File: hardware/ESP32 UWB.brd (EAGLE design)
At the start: 72.3 x 32.6 mm, 54 parts, among them J2 HEADER-12P-2.54, J4 10118194-0001LF, Q3 S8050, Q4 S8050, U1 SILICON_LABS_CP2102N-A01-GQFN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, U2 V_REG_MIC2920, U5 DWM1000, U6 ESP32-C3-MINI-1-N4

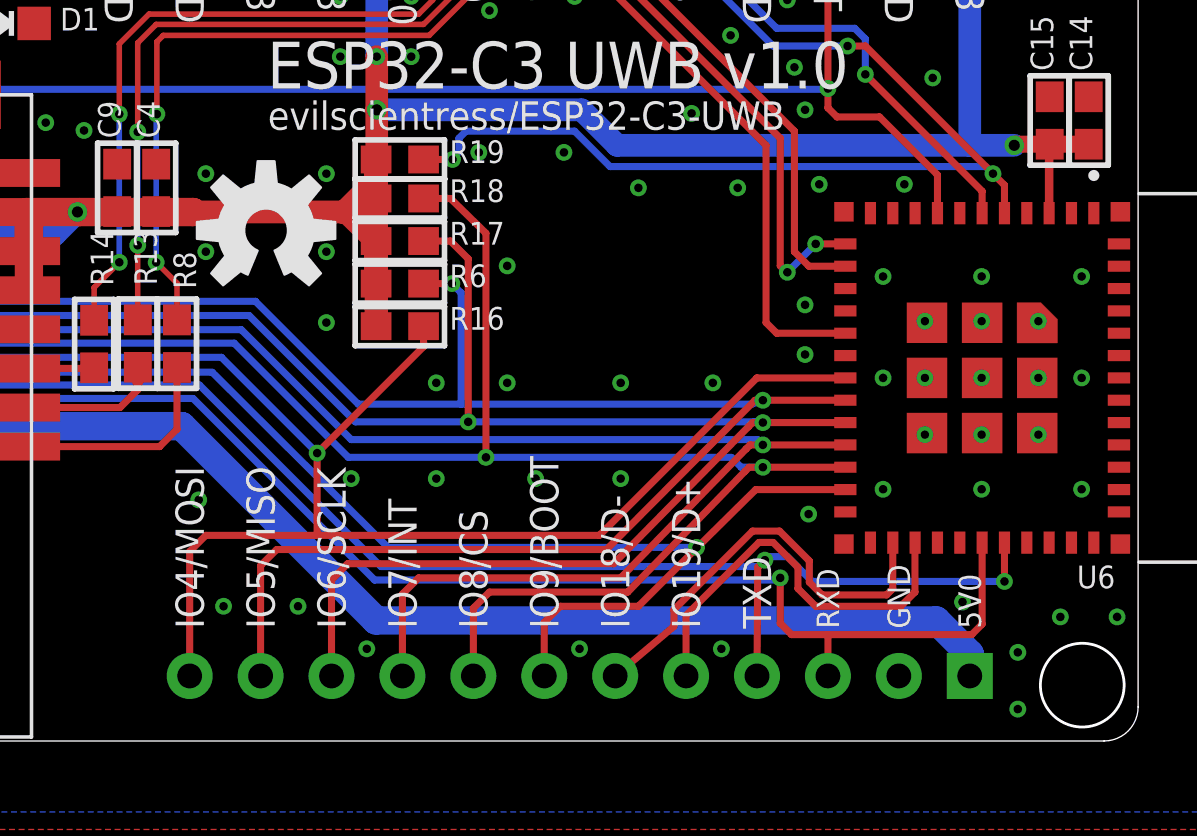
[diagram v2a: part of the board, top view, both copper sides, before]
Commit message: Added WS2812b led for status display
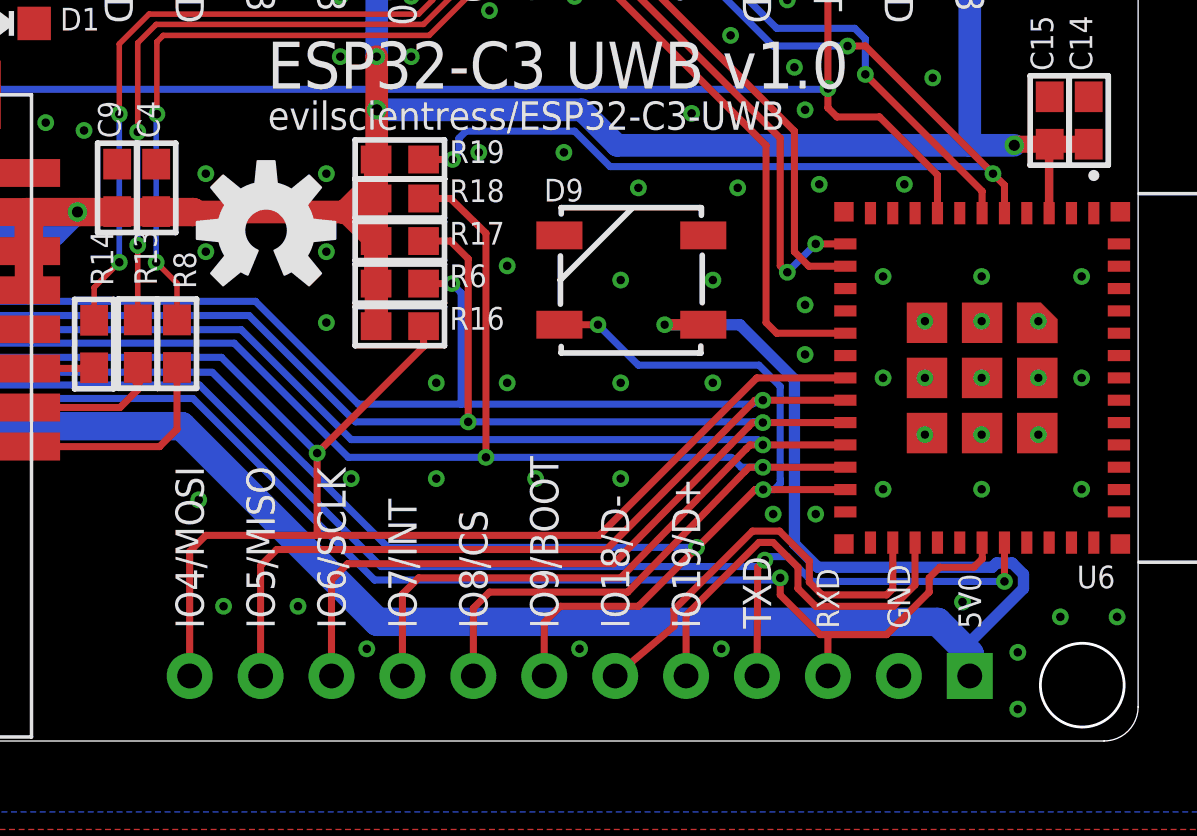
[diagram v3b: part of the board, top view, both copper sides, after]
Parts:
- added D9: (no value), SparkFun-LED:WS2812B
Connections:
- net GND: now also D9.3
- net IO9: now also D9.4
- net VDD5V: now also D9.1
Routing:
- net VDD5V: track 70.3 -> 95.5 mm, vias 1 -> 2
- net IO9: track 83.9 -> 96.9 mm, vias 2 -> 4
- net RXD: track 70.9 -> 69.2 mm
- net GND: vias 134 -> 137
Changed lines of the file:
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@@
 <setting verticaltext="up"/>
 </settings>
-<grid distance="10" unitdist="mil" unit="mil" style="dots" multiple="1" display="yes" altdistance="1" altunitdist="mil" altunit="mil"/>
+<grid distance="10" unitdist="mil" unit="mm" style="dots" multiple="1" display="yes" altdistance="1" altunitdist="mil" altunit="mil"/>
 <layers>
 <layer number="1" name="Top" color="4" fill="1" visible="yes" active="yes"/>
@@
 <attribute name="VALUE" x="3.81" y="10.16" size="0.4064" layer="27" font="vector" ratio="10" rot="R180"/>
 </element>
+<element name="D9" library="SparkFun-LED" package="WS2812B" value="" x="53.848" y="16.51" smashed="yes" rot="R180">
+<attribute name="PROD_ID" value="DIO-12503" x="53.848" y="16.51" size="1.016" layer="27" font="vector" ratio="18" rot="R180" display="off"/>
+<attribute name="NAME" x="52.134" y="20.136" size="0.8128" layer="25" font="vector" ratio="18" rot="R180"/>
+<attribute name="VALUE" x="49.594" y="18.11" size="0.6096" layer="27" rot="R180"/>
+</element>
 </elements>
 <signals>
@@
 <via x="7.493" y="20.193" extent="1-16" drill="0.3048"/>
 <via x="10.16" y="12.954" extent="1-16" drill="0.3048"/>
-<via x="60.198" y="8.128" extent="1-16" drill="0.3048"/>
+<via x="60.452" y="8.128" extent="1-16" drill="0.3048"/>
 <via x="65.7098" y="4.9784" extent="1-16" drill="0.3048"/>
 <via x="71.247" y="4.445" extent="1-16" drill="0.3048"/>
@@
 <contactref element="C5" pad="2"/>
 <contactref element="C7" pad="2"/>
+<contactref element="D9" pad="3"/>
+<via x="58.928" y="8.128" extent="1-16" drill="0.3048"/>
+<via x="56.769" y="16.51" extent="1-16" drill="0.3048"/>
+<via x="53.467" y="16.51" extent="1-16" drill="0.3048"/>
 </signal>
 <signal name="+3V3">
@@
 <wire x1="59.817" y1="6.223" x2="59.817" y2="5.461" width="0.254" layer="1"/>
 <wire x1="59.817" y1="5.461" x2="60.452" y2="4.826" width="0.254" layer="1"/>
-<wire x1="60.452" y1="4.826" x2="63.5" y2="4.826" width="0.254" layer="1"/>
-<wire x1="63.5" y1="4.826" x2="64.008" y2="5.334" width="0.254" layer="1"/>
-<wire x1="64.008" y1="5.334" x2="64.008" y2="7.0994" width="0.254" layer="1"/>
+<wire x1="60.452" y1="4.826" x2="63.246" y2="4.826" width="0.254" layer="1"/>
+<wire x1="63.246" y1="4.826" x2="64.008" y2="5.588" width="0.254" layer="1"/>
+<wire x1="64.008" y1="5.588" x2="64.008" y2="7.0994" width="0.254" layer="1"/>
 <wire x1="64.008" y1="7.0994" x2="64.0134" y2="7.1048" width="0.254" layer="1"/>
 </signal>
@@
 <wire x1="59.1058" y1="5.7658" x2="59.182" y2="5.842" width="0.254" layer="16"/>
 <via x="59.182" y="5.842" extent="1-16" drill="0.3048"/>
-<wire x1="59.182" y1="4.216" x2="59.182" y2="5.842" width="0.254" layer="1"/>
-<wire x1="66.4134" y1="7.1048" x2="66.4134" y2="4.1834" width="0.254" layer="1"/>
-<wire x1="66.4134" y1="4.1834" x2="66.04" y2="3.81" width="0.254" layer="1"/>
-<wire x1="66.04" y1="3.81" x2="60.89" y2="3.81" width="0.254" layer="1"/>
-<wire x1="60.89" y1="3.81" x2="59.588" y2="3.81" width="0.254" layer="1"/>
-<wire x1="59.182" y1="4.216" x2="59.588" y2="3.81" width="0.254" layer="1"/>
+<wire x1="59.182" y1="5.232" x2="59.182" y2="5.842" width="0.254" layer="1"/>
+<wire x1="66.4134" y1="7.1048" x2="66.421" y2="6.5278" width="0.254" layer="1"/>
+<wire x1="66.421" y1="6.5278" x2="66.1162" y2="6.223" width="0.254" layer="1"/>
+<wire x1="66.1162" y1="6.223" x2="64.897" y2="6.223" width="0.254" layer="1"/>
+<wire x1="64.897" y1="6.223" x2="64.516" y2="5.842" width="0.254" layer="1"/>
+<wire x1="64.516" y1="5.842" x2="64.516" y2="5.334" width="0.254" layer="1"/>
+<wire x1="64.516" y1="5.334" x2="62.992" y2="3.81" width="0.254" layer="1"/>
+<wire x1="62.992" y1="3.81" x2="60.89" y2="3.81" width="0.254" layer="1"/>
+<wire x1="60.89" y1="3.81" x2="60.604" y2="3.81" width="0.254" layer="1"/>
+<wire x1="59.182" y1="5.232" x2="60.604" y2="3.81" width="0.254" layer="1"/>
 <wire x1="60.89" y1="2.33" x2="60.89" y2="3.81" width="0.254" layer="1"/>
 <contactref element="U1" pad="26"/>
@@
 <contactref element="J2" pad="1"/>
 <via x="13.182346875" y="8.77696875" extent="1-16" drill="0.4"/>
-<wire x1="64.77" y1="4.318" x2="44.704" y2="4.318" width="1.016" layer="16"/>
-<wire x1="44.704" y1="4.318" x2="37.7444" y2="11.2776" width="1.016" layer="16"/>
+<wire x1="64.8208" y1="4.2672" x2="44.7548" y2="4.2672" width="1.016" layer="16"/>
+<wire x1="44.7548" y1="4.2672" x2="37.7444" y2="11.2776" width="1.016" layer="16"/>
 <wire x1="37.7444" y1="11.2776" x2="15.682978125" y2="11.2776" width="1.016" layer="16"/>
 <wire x1="9.560475" y1="8.77696875" x2="13.182346875" y2="8.77696875" width="1.016" layer="1"/>
 <wire x1="65.97" y1="2.33" x2="65.97" y2="3.118" width="1.016" layer="16"/>
-<wire x1="65.97" y1="3.118" x2="64.77" y2="4.318" width="1.016" layer="16"/>
+<wire x1="65.97" y1="3.118" x2="64.8208" y2="4.2672" width="1.016" layer="16"/>
 <wire x1="13.182346875" y1="8.77696875" x2="15.682978125" y2="11.2776" width="1.016" layer="16"/>
 <contactref element="U2" pad="1"/>
@@
 <contactref element="C3" pad="1"/>
 <contactref element="D6" pad="-"/>
+<contactref element="D9" pad="1"/>
+<wire x1="56.425" y1="14.91" x2="55.042" y2="14.91" width="0.4064" layer="1"/>
+<via x="55.042" y="14.91" extent="1-16" drill="0.3"/>
+<wire x1="55.042" y1="14.91" x2="57.734" y2="14.91" width="0.4064" layer="16"/>
+<wire x1="57.734" y1="14.91" x2="59.69" y2="12.954" width="0.4064" layer="16"/>
+<wire x1="59.69" y1="12.954" x2="59.69" y2="7.0612" width="0.4064" layer="16"/>
+<wire x1="59.69" y1="7.0612" x2="60.5282" y2="6.223" width="0.4064" layer="16"/>
+<wire x1="60.5282" y1="6.223" x2="66.7766" y2="6.223" width="0.4064" layer="16"/>
+<wire x1="66.7766" y1="6.223" x2="66.929" y2="6.3754" width="0.4064" layer="16"/>
+<wire x1="66.929" y1="6.3754" x2="67.4878" y2="6.3754" width="0.4064" layer="16"/>
+<wire x1="67.4878" y1="6.3754" x2="67.8942" y2="5.969" width="0.4064" layer="16"/>
+<wire x1="67.8942" y1="5.969" x2="67.8942" y2="5.461" width="0.4064" layer="16"/>
+<wire x1="67.8942" y1="5.461" x2="65.97" y2="3.5368" width="0.4064" layer="16"/>
+<wire x1="65.97" y1="3.5368" x2="65.97" y2="3.118" width="0.4064" layer="16"/>
 <wire x1="6.412" y1="5.779" x2="6.417" y2="5.774" width="0" layer="19" extent="1-1"/>
 <wire x1="4.699" y1="5.0428" x2="4.775" y2="5.0292" width="0" layer="19" extent="1-1"/>
@@
 <contactref element="J2" pad="7"/>
 <wire x1="7.092" y1="27.9598" x2="7.004" y2="27.9212" width="0.254" layer="1"/>
-<wire x1="61.5134" y1="9.0048" x2="58.3058" y2="9.0048" width="0.254" layer="1"/>
-<wire x1="58.3058" y1="9.0048" x2="56.1975" y2="6.9215" width="0.254" layer="1"/>
+<wire x1="61.5134" y1="9.0048" x2="58.5724" y2="9.0048" width="0.254" layer="1"/>
+<wire x1="58.2804" y1="9.0048" x2="56.1975" y2="6.9215" width="0.254" layer="1"/>
 <wire x1="56.1975" y1="6.9215" x2="54.102" y2="4.826" width="0.254" layer="1"/>
 <wire x1="54.102" y1="4.826" x2="51.308" y2="4.826" width="0.254" layer="1"/>
@@
 <via x="15.0114" y="24.3586" extent="1-16" drill="0.3"/>
 <wire x1="8.9264" y1="29.1068" x2="14.0732" y2="29.1068" width="0.2" layer="1"/>
+<contactref element="D9" pad="4"/>
+<wire x1="51.271" y1="14.91" x2="52.654" y2="14.91" width="0.254" layer="1"/>
+<wire x1="52.654" y1="14.91" x2="54.102" y2="13.462" width="0.254" layer="16"/>
+<wire x1="54.102" y1="13.462" x2="58.42" y2="13.462" width="0.254" layer="16"/>
+<wire x1="58.42" y1="13.462" x2="59.182" y2="12.7" width="0.254" layer="16"/>
+<wire x1="59.182" y1="12.7" x2="59.182" y2="9.3604" width="0.254" layer="16"/>
+<wire x1="59.182" y1="9.3604" x2="59.182" y2="9.2202" width="0.254" layer="16"/>
+<wire x1="59.182" y1="9.2202" x2="58.9666" y2="9.0048" width="0.254" layer="16"/>
+<wire x1="58.9666" y1="9.0048" x2="58.5724" y2="9.0048" width="0.254" layer="16"/>
+<via x="52.654" y="14.91" extent="1-16" drill="0.3"/>
+<via x="58.5724" y="9.0048" extent="1-16" drill="0.3"/>
+<wire x1="58.2804" y1="9.0048" x2="58.5724" y2="9.0048" width="0.254" layer="1"/>
 </signal>
 <signal name="IO10">

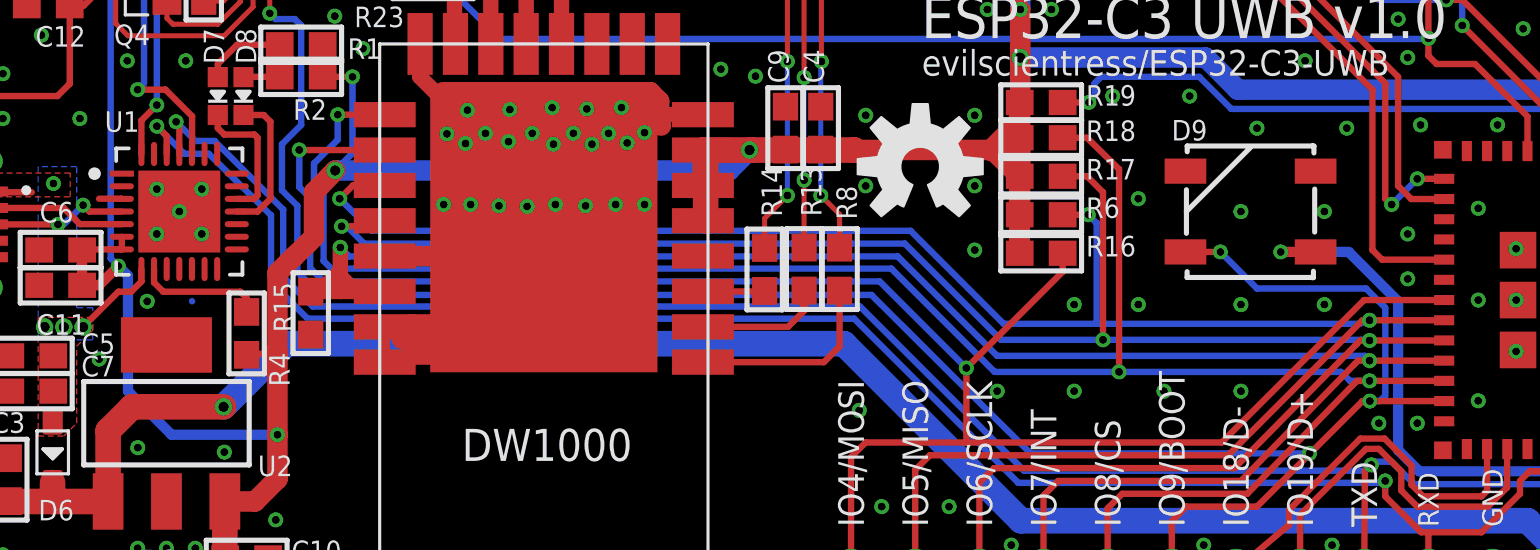
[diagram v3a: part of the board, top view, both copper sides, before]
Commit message: fixed floating input pins
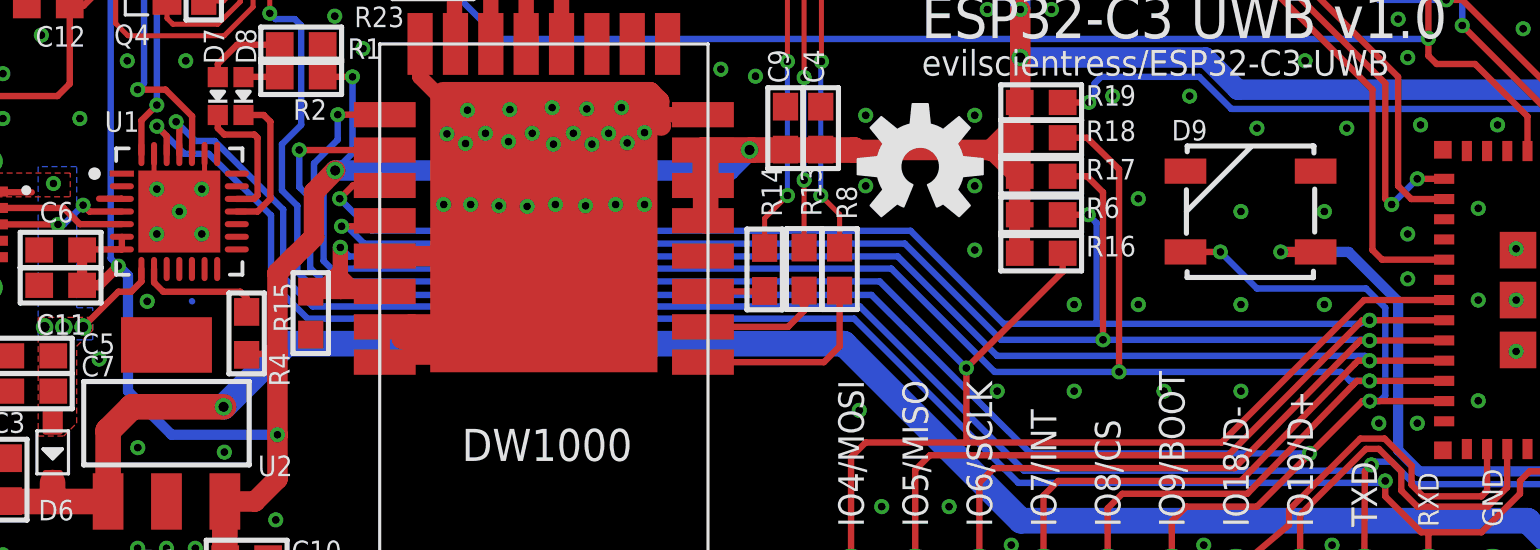
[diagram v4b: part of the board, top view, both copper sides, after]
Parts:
- D9: value (none) -> WS2812B
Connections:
- net GND: now also U1.2, U1.23, U1.27
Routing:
- net GND: track 41.3 -> 44.3 mm
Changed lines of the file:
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@@
 <attribute name="VALUE" x="3.81" y="10.16" size="0.4064" layer="27" font="vector" ratio="10" rot="R180"/>
 </element>
-<element name="D9" library="SparkFun-LED" package="WS2812B" value="" x="53.848" y="16.51" smashed="yes" rot="R180">
+<element name="D9" library="SparkFun-LED" package="WS2812B" value="WS2812B" x="53.848" y="16.51" smashed="yes" rot="R180">
 <attribute name="PROD_ID" value="DIO-12503" x="53.848" y="16.51" size="1.016" layer="27" font="vector" ratio="18" rot="R180" display="off"/>
 <attribute name="NAME" x="52.134" y="20.136" size="0.8128" layer="25" font="vector" ratio="18" rot="R180"/>
@@
 <via x="56.769" y="16.51" extent="1-16" drill="0.3048"/>
 <via x="53.467" y="16.51" extent="1-16" drill="0.3048"/>
+<contactref element="U1" pad="2"/>
+<contactref element="U1" pad="23"/>
+<contactref element="U1" pad="27"/>
+<wire x1="10.43" y1="18.786" x2="10.43" y2="17.399" width="0.2" layer="1"/>
+<wire x1="10.43" y1="17.399" x2="10.541" y2="17.399" width="0.2" layer="1"/>
+<wire x1="12.43" y1="18.786" x2="12.43" y2="17.399" width="0.2" layer="1"/>
+<wire x1="12.43" y1="17.399" x2="12.319" y2="17.399" width="0.2" layer="1"/>
 </signal>
 <signal name="+3V3">
@@
 <wire x1="54.102" y1="13.462" x2="58.42" y2="13.462" width="0.254" layer="16"/>
 <wire x1="58.42" y1="13.462" x2="59.182" y2="12.7" width="0.254" layer="16"/>
-<wire x1="59.182" y1="12.7" x2="59.182" y2="9.3604" width="0.254" layer="16"/>
-<wire x1="59.182" y1="9.3604" x2="59.182" y2="9.2202" width="0.254" layer="16"/>
+<wire x1="59.182" y1="12.7" x2="59.182" y2="9.2202" width="0.254" layer="16"/>
 <wire x1="59.182" y1="9.2202" x2="58.9666" y2="9.0048" width="0.254" layer="16"/>
 <wire x1="58.9666" y1="9.0048" x2="58.5724" y2="9.0048" width="0.254" layer="16"/>
